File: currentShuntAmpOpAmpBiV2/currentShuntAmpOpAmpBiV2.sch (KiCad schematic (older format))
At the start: 11 parts, among them Q1 2N3906, U1 AD822A

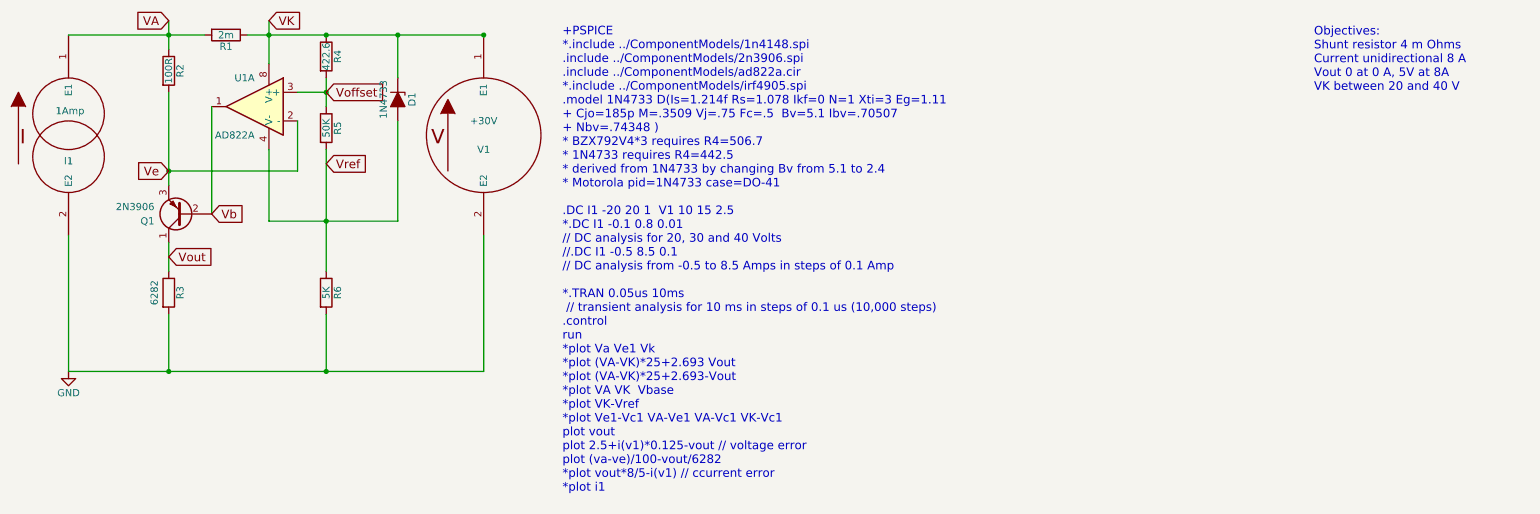
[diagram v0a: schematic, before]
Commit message: completed first bidirectional current monitor; made a second version V2
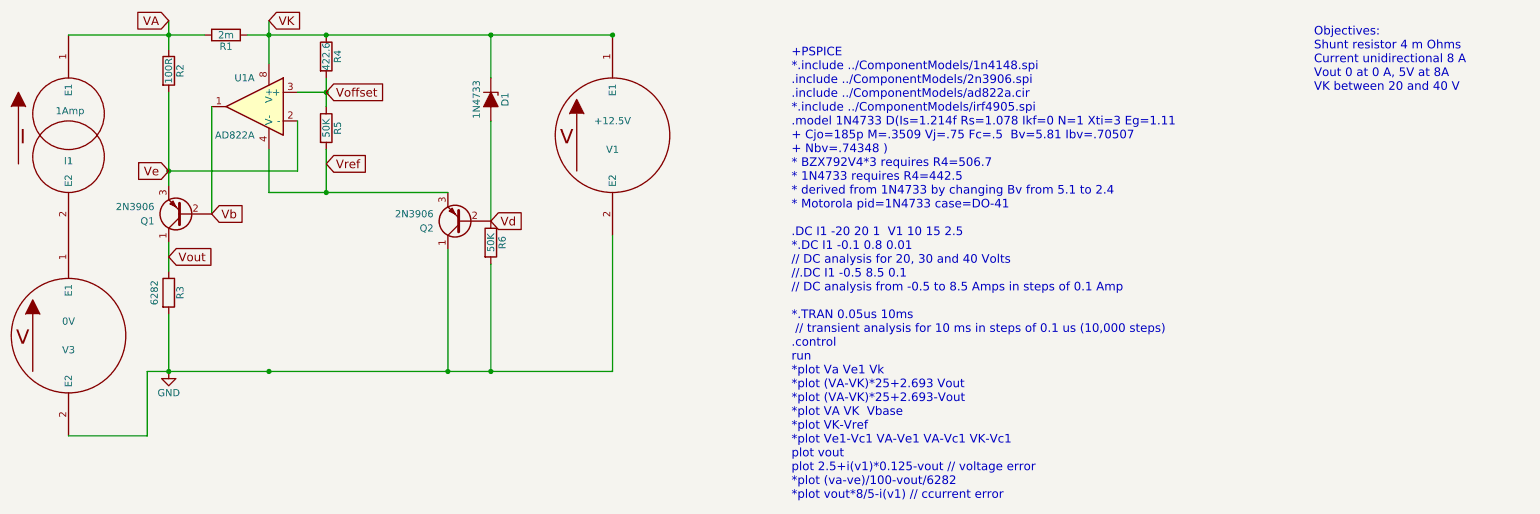
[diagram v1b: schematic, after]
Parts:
- added Q2: 2N3906, symbol Q_PNP_CBE
- added V3: 0V, symbol VSOURCE
- R6: value 5K -> 50K
- V1: value +30V -> +12.5V
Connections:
- net GND: now also Q2.1 (C), V3.2 (E2); no longer I1.2 (E2)
- net Vref: now also Q2.3 (E); no longer D1.2 (A), R6.1
- new net: I1.2 (E2), V3.1 (E1)
- new net Vd: D1.2 (A), Q2.2 (B), R6.1
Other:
- note added: "+PSPICE \n*.include ../ComponentModels/1n4148.spi\n.include ../ComponentModels/2n3906.spi\n.include ../ComponentModels/ad822a.cir\n*.include ../ComponentModels/irf4905.spi\n.model 1N4733 D(Is=1.214f Rs=1.078 Ikf=0 N=1 Xti=3 Eg=1.11\n+ Cjo=185p M=.3509 Vj=.75 Fc=.5 Bv=5.81 Ibv=.70507\n+ Nbv=.74348 )\n* BZX792V4*3 requires R4=506.7\n* 1N4733 requires R4=442.5\n* derived from 1N4733 by changing Bv f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"
- note removed: "+PSPICE \n*.include ../ComponentModels/1n4148.spi\n.include ../ComponentModels/2n3906.spi\n.include ../ComponentModels/ad822a.cir\n*.include ../ComponentModels/irf4905.spi\n.model 1N4733 D(Is=1.214f Rs=1.078 Ikf=0 N=1 Xti=3 Eg=1.11\n+ Cjo=185p M=.3509 Vj=.75 Fc=.5 Bv=5.1 Ibv=.70507\n+ Nbv=.74348 )\n* BZX792V4*3 requires R4=506.7\n* 1N4733 requires R4=442.5\n* derived from 1N4733 by changing Bv fr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"
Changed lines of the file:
@@
 LIBS:contrib
 LIBS:valves
-LIBS:currentShuntAmpOpAmpBi-cache
+LIBS:currentShuntAmpOpAmpBiV2-cache
 EELAYER 25 0
 EELAYER END
@@
 $Comp
 L GND #PWR01
-U 1 1 5AF406F9
-P 900 3050
-F 0 "#PWR01" H 900 2800 50  0001 C CNN
-F 1 "GND" H 900 2900 50  0000 C CNN
-F 2 "" H 900 3050 50  0001 C CNN
-F 3 "" H 900 3050 50  0001 C CNN
-	1    900  3050
-	1    0    0    -1
-$EndComp
-Text Notes 4350 3900 0    60   ~ 0
-+PSPICE \n*.include ../ComponentModels/1n4148.spi\n.include ../ComponentModels/2n3906.spi\n.include ../ComponentModels/ad822a.cir\n*.include ../ComponentModels/irf4905.spi\n.model 1N4733 D(Is=1.214f Rs=1.078 Ikf=0 N=1 Xti=3 Eg=1.11\n+ Cjo=185p M=.3509 Vj=.75 Fc=.5  Bv=5.1 Ibv=.70507\n+ Nbv=.74348 )\n* BZX792V4*3 requires R4=506.7\n* 1N4733 requires R4=442.5\n* derived from 1N4733 by changing Bv from 5.1 to 2.4\n* Motorola pid=1N4733 case=DO-41\n\n.DC I1 -20 20 1  V1 10 15 2.5 \n*.DC I1 -0.1 0.8 0.01  \n// DC analysis for 20, 30 and 40 Volts\n//.DC I1 -0.5 8.5 0.1\n// DC analysis from -0.5 to 8.5 Amps in steps of 0.1 Amp\n\n*.TRAN 0.05us 10ms\n // transient analysis for 10 ms in steps of 0.1 us (10,000 steps)\n.control\nrun\n*plot Va Ve1 Vk\n*plot (VA-VK)*25+2.693 Vout\n*plot (VA-VK)*25+2.693-Vout\n*plot VA VK  Vbase\n*plot VK-Vref\n*plot Ve1-Vc1 VA-Ve1 VA-Vc1 VK-Vc1\nplot vout\nplot 2.5+i(v1)*0.125-vout // voltage error\nplot (va-ve)/100-vout/6282\n*plot vout*8/5-i(v1) // ccurrent error\n*plot i1\n
+U 1 1 5AF50EDE
+P 1600 3050
+F 0 "#PWR01" H 1600 2800 50  0001 C CNN
+F 1 "GND" H 1600 2900 50  0000 C CNN
+F 2 "" H 1600 3050 50  0001 C CNN
+F 3 "" H 1600 3050 50  0001 C CNN
+	1    1600 3050
+	1    0    0    -1
+$EndComp
+Text Notes 5950 3950 0    60   ~ 0
++PSPICE \n*.include ../ComponentModels/1n4148.spi\n.include ../ComponentModels/2n3906.spi\n.include ../ComponentModels/ad822a.cir\n*.include ../ComponentModels/irf4905.spi\n.model 1N4733 D(Is=1.214f Rs=1.078 Ikf=0 N=1 Xti=3 Eg=1.11\n+ Cjo=185p M=.3509 Vj=.75 Fc=.5  Bv=5.81 Ibv=.70507\n+ Nbv=.74348 )\n* BZX792V4*3 requires R4=506.7\n* 1N4733 requires R4=442.5\n* derived from 1N4733 by changing Bv from 5.1 to 2.4\n* Motorola pid=1N4733 case=DO-41\n\n.DC I1 -20 20 1  V1 10 15 2.5 \n*.DC I1 -0.1 0.8 0.01  \n// DC analysis for 20, 30 and 40 Volts\n//.DC I1 -0.5 8.5 0.1\n// DC analysis from -0.5 to 8.5 Amps in steps of 0.1 Amp\n\n*.TRAN 0.05us 10ms\n // transient analysis for 10 ms in steps of 0.1 us (10,000 steps)\n.control\nrun\n*plot Va Ve1 Vk\n*plot (VA-VK)*25+2.693 Vout\n*plot (VA-VK)*25+2.693-Vout\n*plot VA VK  Vbase\n*plot VK-Vref\n*plot Ve1-Vc1 VA-Ve1 VA-Vc1 VK-Vc1\nplot vout\nplot 2.5+i(v1)*0.125-vout // voltage error\n*plot (va-ve)/100-vout/6282\n*plot vout*8/5-i(v1) // ccurrent error\n
 Connection ~ 2300 700
 $Comp
 L VSOURCE V1
-U 1 1 5AF406FA
-P 3800 1400
-F 0 "V1" H 3800 1300 50  0000 C CNN
-F 1 "+30V " H 3800 1500 50  0000 C CNN
-F 2 "" H 3800 1400 50  0001 C CNN
-F 3 "" H 3800 1400 50  0001 C CNN
-	1    3800 1400
+U 1 1 5AF50EDF
+P 4700 1400
+F 0 "V1" H 4700 1300 50  0000 C CNN
+F 1 "+12.5V " H 4700 1500 50  0000 C CNN
+F 2 "" H 4700 1400 50  0001 C CNN
+F 3 "" H 4700 1400 50  0001 C CNN
+	1    4700 1400
 	1    0    0    -1
 $EndComp
@@
 Connection ~ 1600 700
 Wire Wire Line
-	900  2100 900  3050
-Wire Wire Line
-	3800 3050 3800 2100
+	4700 3050 4700 2100
 $Comp
 L ISOURCE I1
-U 1 1 5AF406FB
+U 1 1 5AF50EE0
 P 900 1400
 F 0 "I1" H 900 1220 50  0000 C CNN
@@
 $Comp
 L R R1
-U 1 1 5AF406FC
+U 1 1 5AF50EE1
 P 2000 700
 F 0 "R1" V 2080 700 50  0000 C CNN
@@
 Text Notes 9600 1100 0    60   ~ 0
 Objectives:\nShunt resistor 4 m Ohms\nCurrent unidirectional 8 A\nVout 0 at 0 A, 5V at 8A\nVK between 20 and 40 V
-Connection ~ 3800 700
+Connection ~ 4700 700
 Connection ~ 1600 3050
 Wire Wire Line
-	2150 700  3800 700
-Wire Wire Line
-	900  3050 3800 3050
+	2150 700  4700 700
+Wire Wire Line
+	1450 3050 4700 3050
 $Comp
 L AD8620 U1
-U 1 1 5AF406FD
+U 1 1 5AF50EE2
 P 2200 1200
 F 0 "U1" H 2200 1400 50  0000 L CNN
@@
 $Comp
 L R R2
-U 1 1 5AF406FE
+U 1 1 5AF50EE3
 P 1600 950
 F 0 "R2" V 1680 950 50  0000 C CNN
@@
 $Comp
 L Q_PNP_CBE Q1
-U 1 1 5AF406FF
+U 1 1 5AF50EE4
 P 1700 1950
 F 0 "Q1" H 1900 2000 50  0000 L CNN
@@
 $Comp
 L R R3
-U 1 1 5AF40700
+U 1 1 5AF50EE5
 P 1600 2500
 F 0 "R3" V 1680 2500 50  0000 C CNN
@@
 Wire Wire Line
 	1600 2650 1600 3050
-Connection ~ 2700 3050
 Text GLabel 1600 2250 2    60   Input ~ 0
 Vout
@@
 $Comp
 L R R4
-U 1 1 5AF40703
+U 1 1 5AF50EE6
 P 2700 850
 F 0 "R4" V 2780 850 50  0000 C CNN
@@
 $Comp
 L R R5
-U 1 1 5AF40704
+U 1 1 5AF50EE7
 P 2700 1350
 F 0 "R5" V 2780 1350 50  0000 C CNN
@@
 $Comp
 L D_Zener_ALT D1
-U 1 1 5AF4167E
-P 3200 1150
-F 0 "D1" H 3200 1250 50  0000 C CNN
-F 1 "1N4733" H 3200 1050 50  0000 C CNN
-F 2 "" H 3200 1150 50  0001 C CNN
-F 3 "" H 3200 1150 50  0001 C CNN
-F 4 "2,1" H 3200 1150 60  0001 C CNN "Spice_Node_Sequence"
-	1    3200 1150
+U 1 1 5AF50EE8
+P 3850 1150
+F 0 "D1" H 3850 1250 50  0000 C CNN
+F 1 "1N4733" H 3850 1050 50  0000 C CNN
+F 2 "" H 3850 1150 50  0001 C CNN
+F 3 "" H 3850 1150 50  0001 C CNN
+F 4 "2,1" H 3850 1150 60  0001 C CNN "Spice_Node_Sequence"
+	1    3850 1150
 	0    1    1    0
 $EndComp
 Wire Wire Line
-	3200 1000 3200 700
-Connection ~ 3200 700
-Wire Wire Line
-	3200 2000 3200 1300
+	3850 1000 3850 700
+Connection ~ 3850 700
+Wire Wire Line
+	3850 2000 3850 1300
 $Comp
 L R R6
-U 1 1 5AF41732
-P 2700 2500
-F 0 "R6" V 2780 2500 50  0000 C CNN
-F 1 "5K" V 2700 2500 50  0000 C CNN
-F 2 "" V 2630 2500 50  0001 C CNN
-F 3 "" H 2700 2500 50  0001 C CNN
-	1    2700 2500
-	1    0    0    -1
-$EndComp
-Wire Wire Line
-	2700 3050 2700 2650
+U 1 1 5AF50EE9
+P 3850 2150
+F 0 "R6" V 3930 2150 50  0000 C CNN
+F 1 "50K" V 3850 2150 50  0000 C CNN
+F 2 "" V 3780 2150 50  0001 C CNN
+F 3 "" H 3850 2150 50  0001 C CNN
+	1    3850 2150
+	1    0    0    -1
+$EndComp
 Text GLabel 2700 1100 2    60   Input ~ 0
 Voffset
@@
 Vref
 Wire Wire Line
-	2700 1500 2700 2350
-Wire Wire Line
-	2300 2000 3200 2000
-Wire Wire Line
-	2300 1500 2300 2000
-Connection ~ 2700 2000
+	2300 1500 2300 1800
+Connection ~ 2700 1800
+Connection ~ 2300 3050
+Wire Wire Line
+	2300 1800 3550 1800
+$Comp
+L VSOURCE V3
+U 1 1 5AF52D57
+P 900 2800
+F 0 "V3" H 900 2700 50  0000 C CNN
+F 1 "0V " H 900 2900 50  0000 C CNN
+F 2 "" H 900 2800 50  0001 C CNN
+F 3 "" H 900 2800 50  0001 C CNN
+	1    900  2800
+	1    0    0    -1
+$EndComp
+Wire Wire Line
+	900  3500 1450 3500
+Wire Wire Line
+	1450 3500 1450 3050
+Wire Wire Line
+	3850 2300 3850 3050
+Connection ~ 3850 3050
+$Comp
+L Q_PNP_CBE Q2
+U 1 1 5AF53280
+P 3650 2000
+F 0 "Q2" H 3850 2050 50  0000 L CNN
+F 1 "2N3906" H 3850 1950 50  0000 L CNN
+F 2 "" H 3850 2100 50  0001 C CNN
+F 3 "" H 3650 2000 50  0001 C CNN
+	1    3650 2000
+	-1   0    0    1
+$EndComp
+Wire Wire Line
+	3550 2200 3550 3050
+Connection ~ 3550 3050
+Wire Wire Line
+	2700 1800 2700 1500
+Text GLabel 3850 2000 2    60   Input ~ 0
+Vd
 $EndSCHEMATC
